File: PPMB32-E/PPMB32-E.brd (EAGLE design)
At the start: 81.3 x 88.9 mm, 48 parts, among them IC1 7805TV, IC2 LM3940IT-3.3, K1 ARK500/2, K2 ARK500/2, K3 ARK500/2, K4 ARK500/2, K5 ARK500/2

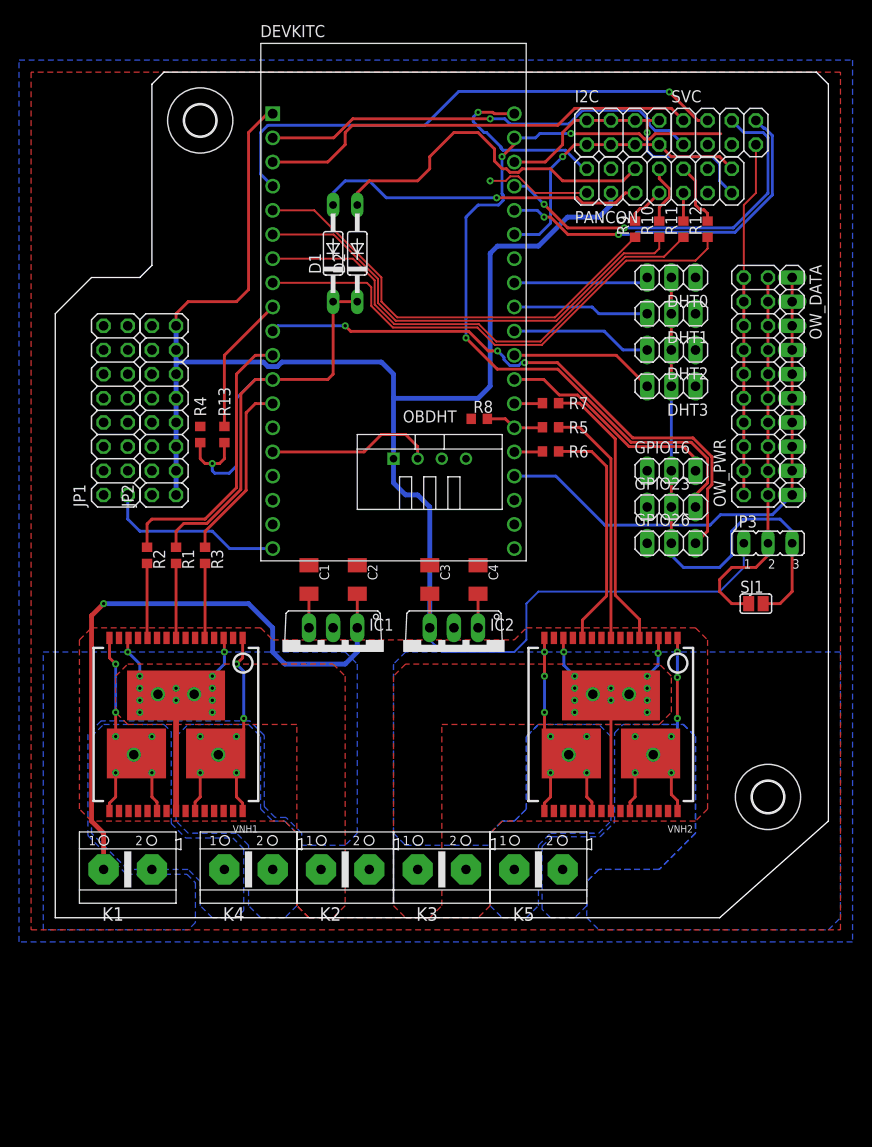
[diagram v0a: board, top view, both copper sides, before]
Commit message: Remove obsolete files, pre-release versions of PPSB-T & PPSB-TH
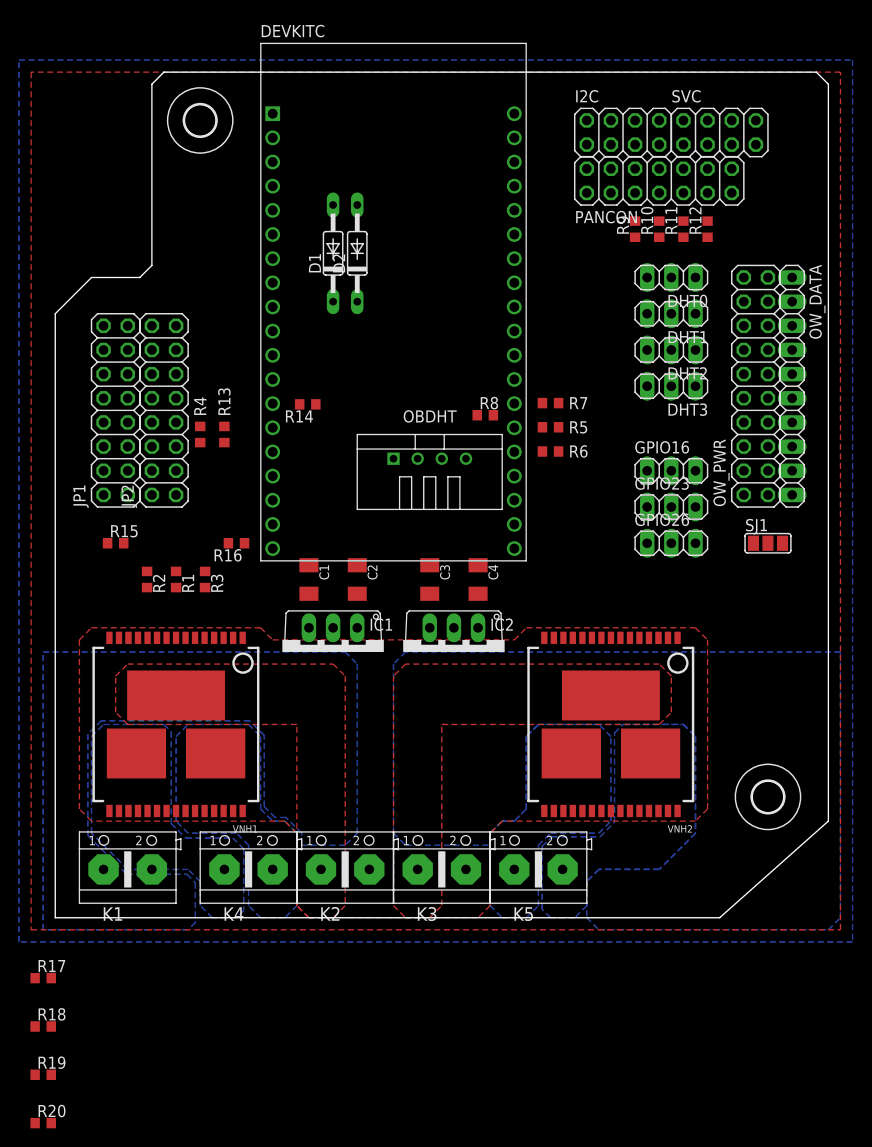
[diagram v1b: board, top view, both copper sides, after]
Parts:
- removed JP3: (no value), jumper:JP2
- added R14, R15, R16, R17, R18, R19, R20: 1k, rcl:R0603
- SJ1: device jumper:SJ -> jumper:SJ_2
- moved SJ1 6.48 mm to (74.9, 39.4)
- moved R1 2.54 mm to (12.7, 35.6)
- moved R2 2.54 mm to (9.65, 35.6)
- moved R3 2.54 mm to (15.7, 35.6)
- moved R8 0.74 mm to (45.2, 52.8)
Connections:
- new net N$12: DEVKITC.12, R14.2
- net +3V3: now also R17.2, R18.2, R19.2, R20.2, SJ1.1; no longer JP3.1
- net +5V: now also SJ1.3; no longer JP3.3, SJ1.2
- net GND: now also R15.1, R16.1
- net GPIO16: no longer DEVKITC.31
- net GPIO23: no longer DEVKITC.21
- net I2C_SDA: now also DEVKITC.21; no longer DEVKITC.25
- net N$11: now also SJ1.2; no longer JP3.2, SJ1.1
- net PANCON_B1: now also R17.1
- net PANCON_B2: now also R18.1
- net PANCON_B3: now also R19.1
- net PANCON_B4: now also R20.1
- net VNH1_INA: now also R16.2
- net VNH1_INB: now also R15.2
- net VNH1_PWM: now also DEVKITC.31, R14.1; no longer DEVKITC.12
- net VNH2_PWM: no longer DEVKITC.33
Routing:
- net +3V3: track 187.9 -> 0.00 mm
- net GPIO23: track 83.1 -> 0.00 mm, vias 3 -> 0
- net VCC: track 66.4 -> 0.00 mm, vias 1 -> 0
- net VNH1_PWM: track 62.9 -> 0.00 mm, vias 1 -> 0
- net GPIO26: track 62.3 -> 0.00 mm, vias 3 -> 0
- net +5V: track 57.7 -> 0.00 mm
- net GND: track 56.5 -> 0.00 mm, vias 1 -> 0
- net SVN: track 56.2 -> 0.00 mm, vias 1 -> 0
- net ONE_WIRE: track 55.5 -> 0.00 mm
- net N$10: track 55.0 -> 0.00 mm
- net N$9: track 52.8 -> 0.00 mm
- net N$8: track 50.2 -> 0.00 mm
- net N$4: track 47.7 -> 0.00 mm
- net SVP: track 46.8 -> 0.00 mm
- net ESP_EN: track 46.6 -> 0.00 mm, vias 1 -> 0
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
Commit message: Improved schematics layout.
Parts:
- added SJ2, SJ3: (no value), jumper:SJ
- D1, D2: value 1N4446 -> BAT85; device diode:DO35-10 -> adafruit:DO35-7
- R10, R11, R12, R9: value 200R -> 270R
- R15, R16, R4, R8: value 1k -> 47k
- moved R20 118.6 mm to (71.1, 72.4), turned to 270 degrees
- moved R19 103.7 mm to (52.1, 72.4), turned to 270 degrees
- moved R18 100.7 mm to (54.6, 72.4), turned to 270 degrees
- moved R17 98.0 mm to (57.1, 72.4), turned to 270 degrees
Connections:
- net PANCON_W1: now also SJ3.2
- net PANCON_W2: now also SJ2.2
- net VNH1_INA: now also SJ3.1
- net VNH1_INB: now also SJ2.1
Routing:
- net SVN: track 0.00 -> 52.1 mm, vias 0 -> 1
- net ESP_EN: track 0.00 -> 50.4 mm
- net SVP: track 0.00 -> 46.6 mm
- net +3V3: track 0.00 -> 45.6 mm
- net UART0_RXD: track 0.00 -> 41.5 mm
- net UART0_TXD: track 0.00 -> 35.3 mm
- net I2C_SCL: track 0.00 -> 31.7 mm
- net I2C_SDA: track 0.00 -> 24.2 mm
- net ONE_WIRE: track 0.00 -> 22.9 mm
- net PANCON_B2: track 0.00 -> 6.70 mm
- net PANCON_B4: track 0.00 -> 6.55 mm
- net PANCON_B1: track 0.00 -> 4.38 mm
- net PANCON_B3: track 0.00 -> 2.96 mm
- net GND: track 0.00 -> 2.54 mm
